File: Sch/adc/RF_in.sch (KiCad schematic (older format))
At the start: 72 parts, among them CN1 SMA, CN2 SMA, J3 JP2, J4 JP2, J5 JP2, J6 JP2, U1 LTC2292, U2 BGA2818, U3 TLV702, U4 BGA2818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

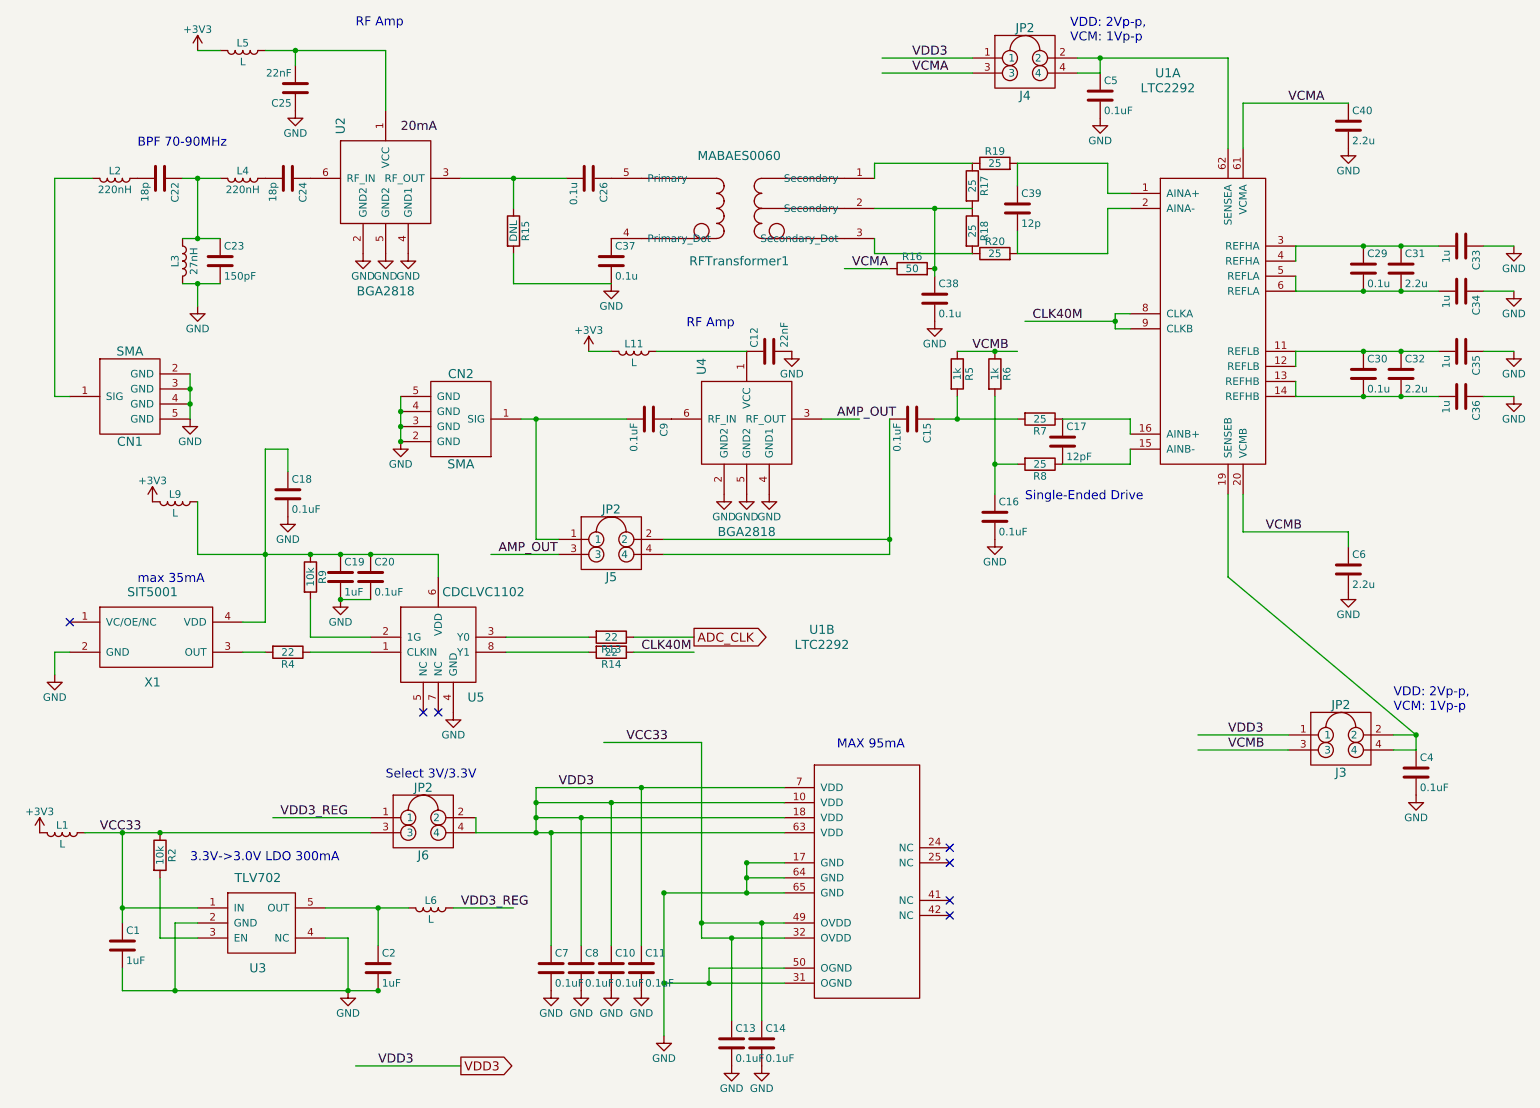
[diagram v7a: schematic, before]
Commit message: Modification in progress. Changed clock gen.
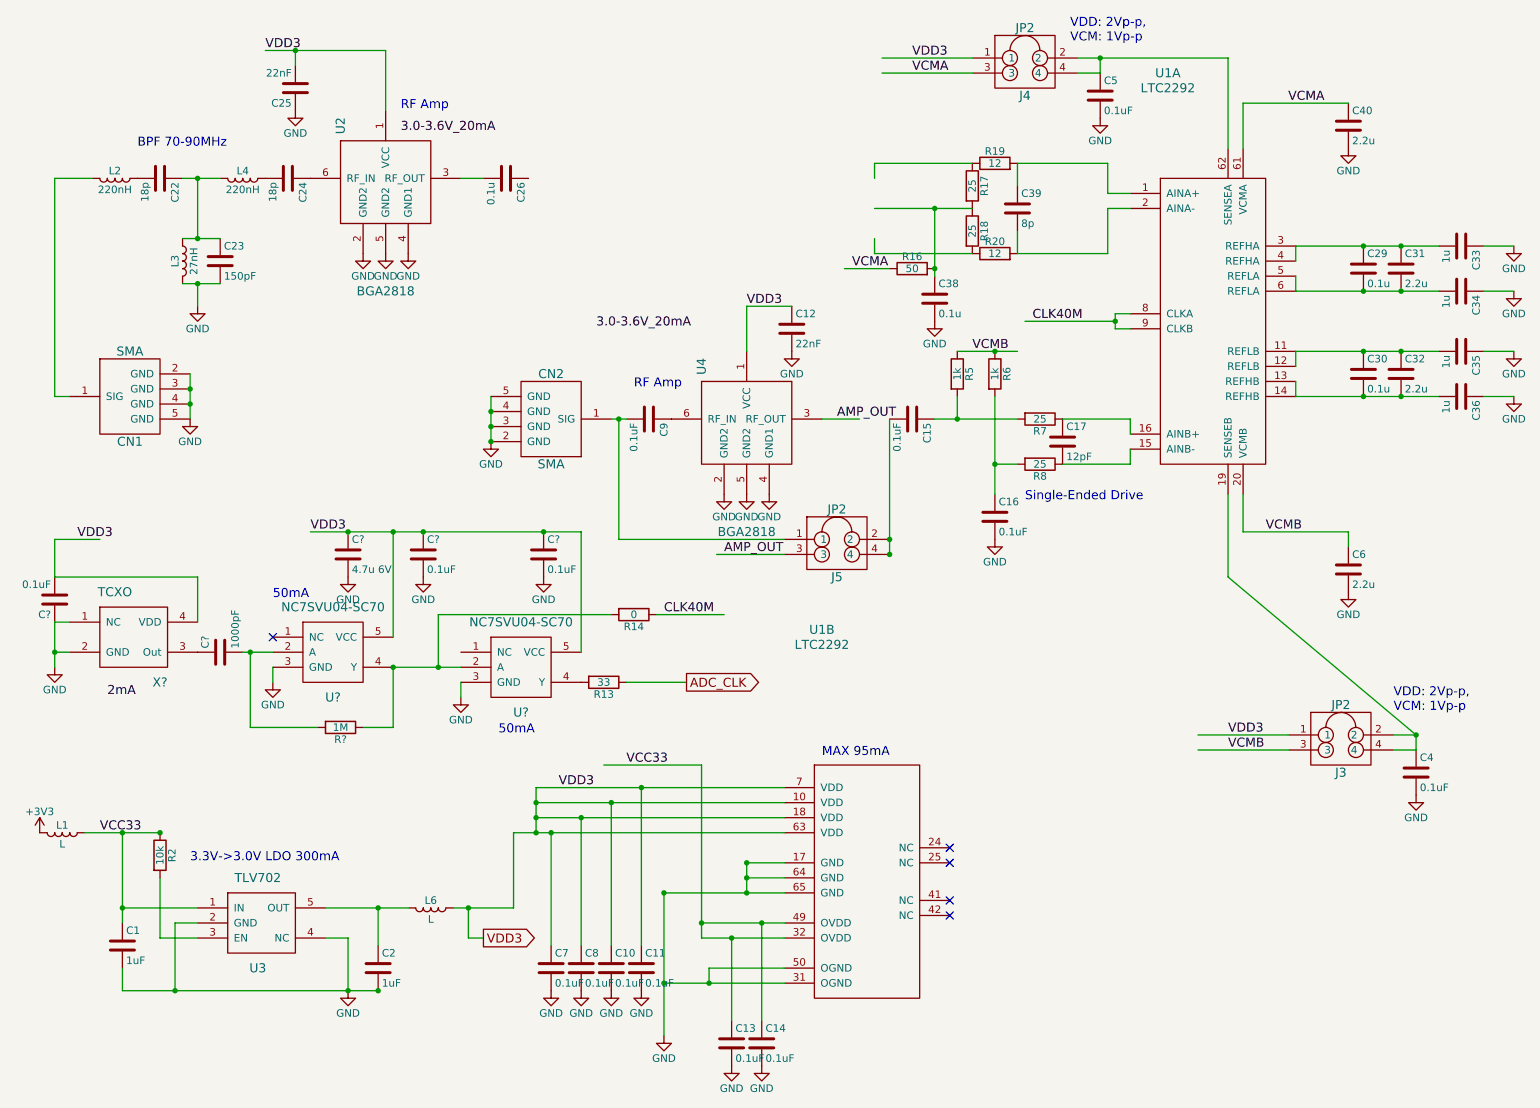
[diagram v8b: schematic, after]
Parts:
- removed C18: 0.1uF, adc_lib:C0402, symbol C
- removed C19: 1uF, adc_lib:C0603, symbol C
- removed C20: 0.1uF, adc_lib:C0603, symbol C
- removed C37: 0.1u, adc_lib:C0603, symbol C
- removed J6: JP2, adc_lib:M20-9980245, symbol JP2
- removed L11, L5, L9: L, adc_lib:FB0805, symbol L
- removed R15: DNL, adc_lib:R0603, symbol R
- removed R4: 22, adc_lib:R0603, symbol R
- removed R9: 10k, adc_lib:R0603, symbol R
- removed RFTransformer1: MABAES0060, adc_lib:MABAES0060, symbol MABAES0060
- removed U5: CDCLVC1102, adc_lib:CDCLVC1102, symbol CDCLVC1102
- removed X1: SIT5001, adc_lib:SIT5001, symbol SIT5001
- added C? (x3): 0.1uF, adc_lib:C0402, symbol C
- added C?: 1000pF, adc_lib:C0402, symbol C
- added C?: 4.7u 6V, adc_lib:C0402, symbol C
- added R?: 1M, symbol R
- added U? (x2): NC7SVU04-SC70, symbol NC7SVU04-SC70
- added X?: TCXO, symbol TCXO
- C39: value 12p -> 8p
- R13: value 22 -> 33
- R14: value 22 -> 0
- R19, R20: value 25 -> 12
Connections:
- net labels added: 2mA, 3.0-3.6V_20mA
- net labels removed: 20mA, VDD3_REG
- wire segments 144 -> 194
- no-connect marks 7 -> 5
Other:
- note added: "50mA"
- note removed: "Select 3V/3.3V"
- note removed: "max 35mA"
- moved on the sheet: C12, C26, CN2, J5, R13, R14
